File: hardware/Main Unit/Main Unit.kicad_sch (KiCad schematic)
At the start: 1 part

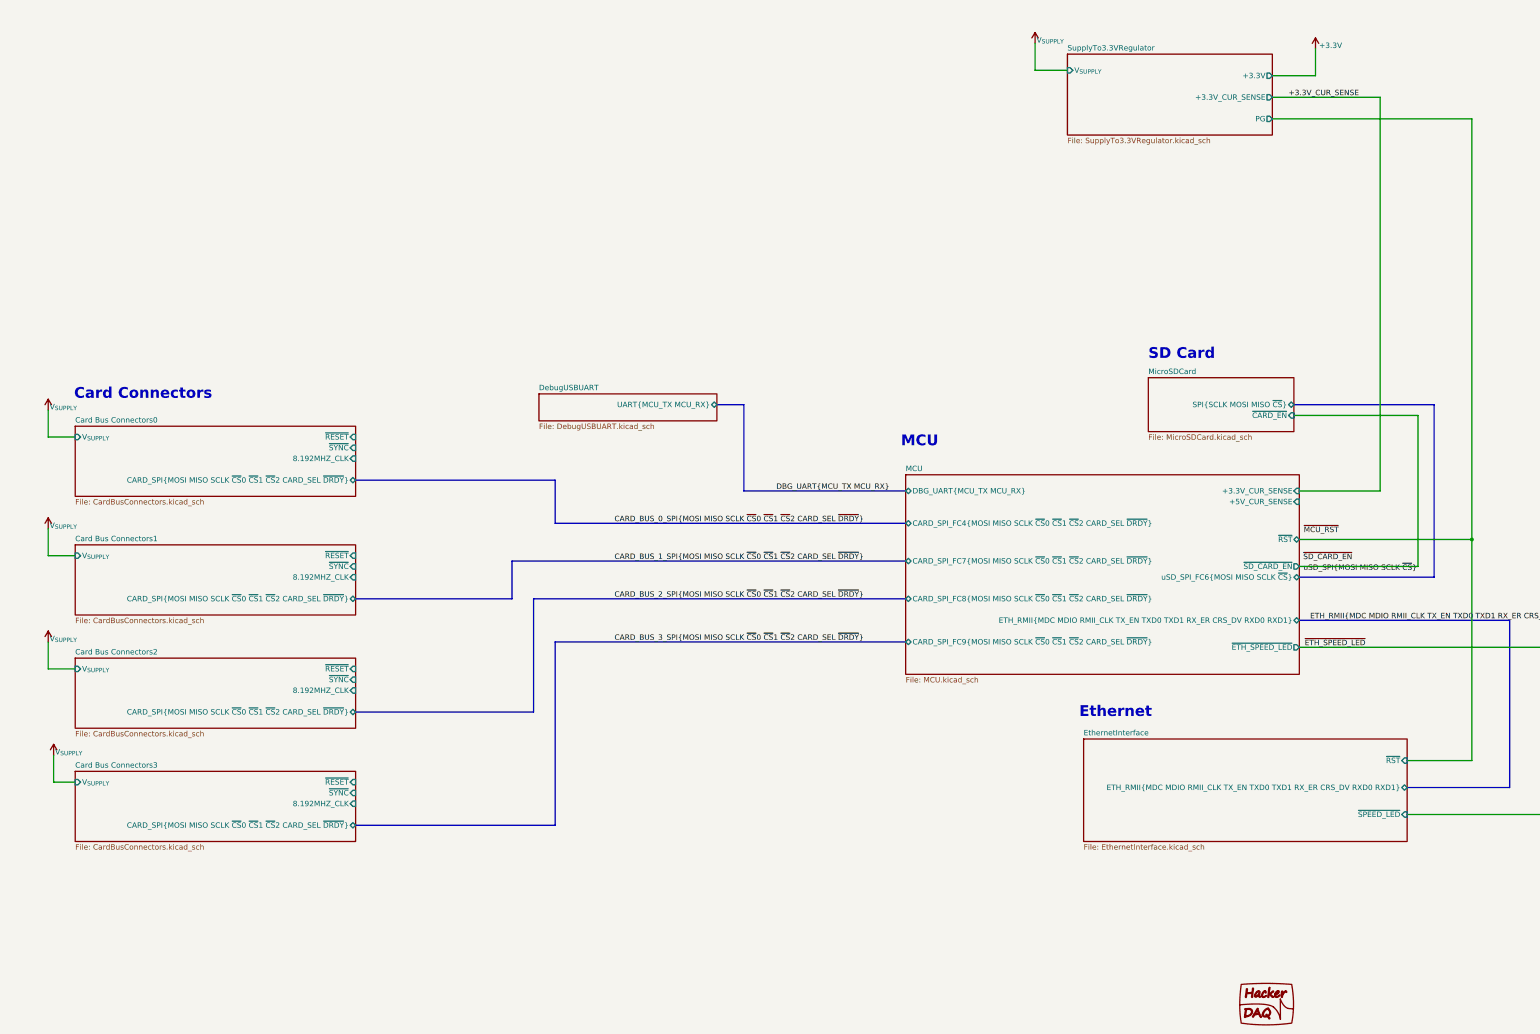
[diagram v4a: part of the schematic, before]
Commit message: Main unit: Add USB port for MCU and 3.3VA rail, start on routing
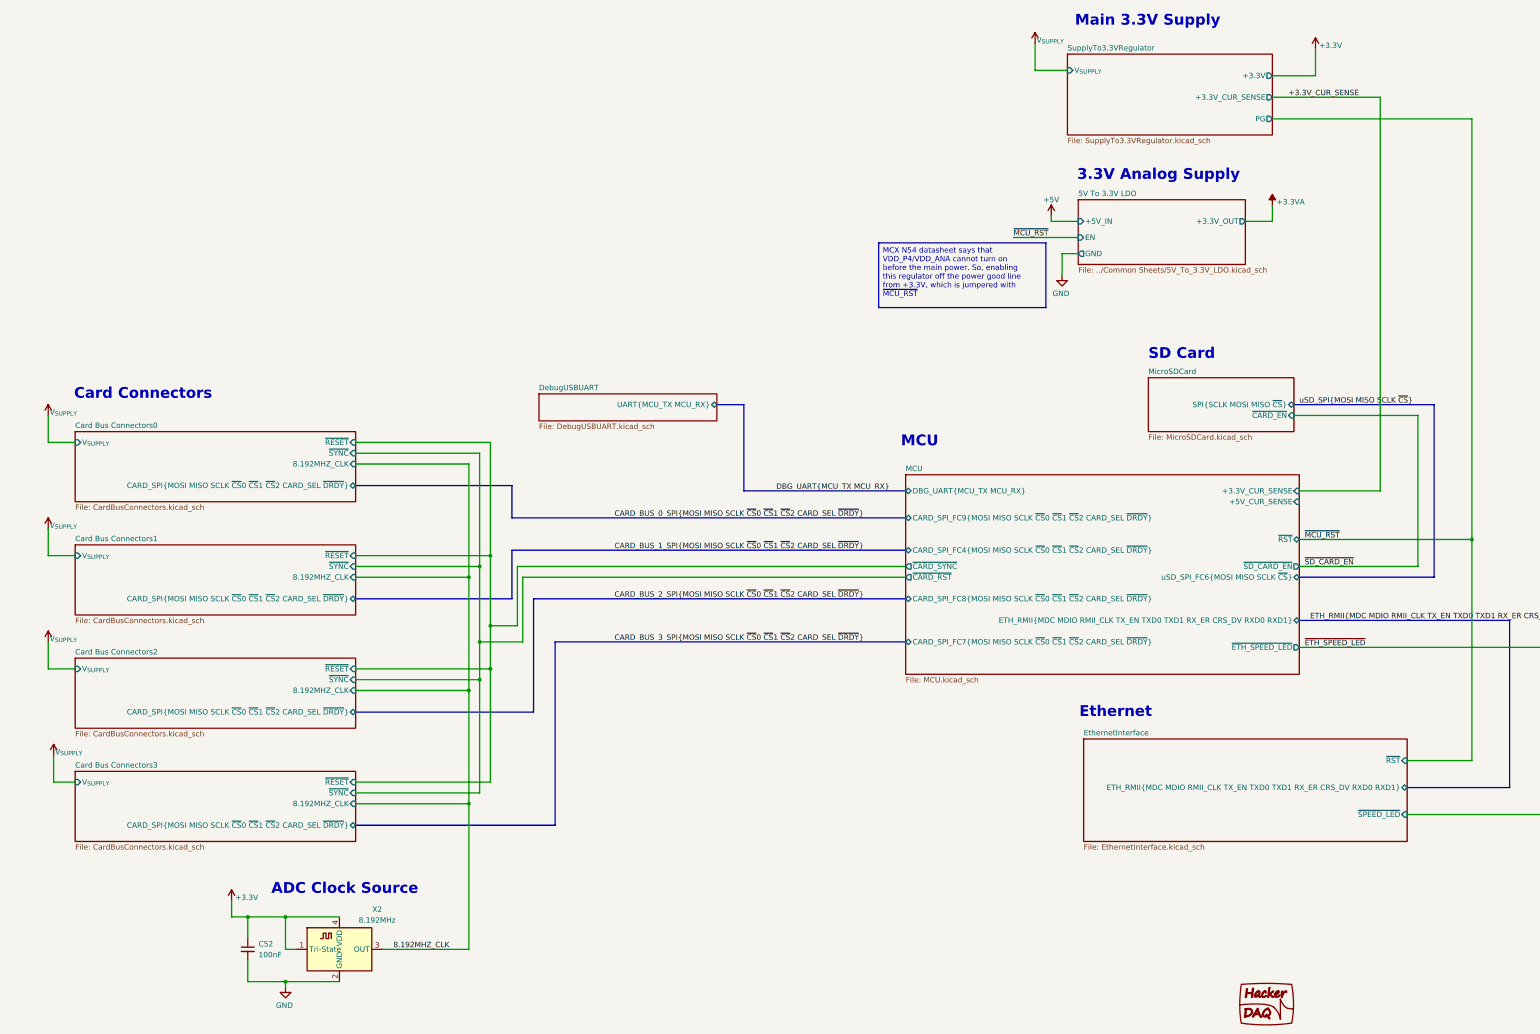
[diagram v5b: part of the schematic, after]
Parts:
- added C52: 100nF, Capacitor_SMD:C_0603_1608Metric, symbol Device:C_Small
- added X2: 8.192MHz, Oscillator:Oscillator_SMD_ECS_2520MV-xxx-xx-4Pin_2.5x2.0mm, symbol Oscillator:ECS-2520MV-xxx-xx
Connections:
- net +3.3V: now also C52.1, X2.1 (Tri-State), X2.4 (VDD)
- new net 8.192MHZ_CLK: X2.3 (OUT)
- new net GND: C52.2, X2.2 (GND)
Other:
- added sheet 5V To 3.3V LDO (../Common Sheets/5V_To_3.3V_LDO.kicad_sch)
- sheet MCU ports: added ~{CARD_RST}, ~{CARD_SYNC}; removed none
- note added: "3.3V Analog Supply"
- note added: "ADC Clock Source"
- note added: "Main 3.3V Supply"

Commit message: Add schematic for Vsupply input
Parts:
- added TP2: +3.3VA, TestPoint:TestPoint_THTPad_D2.5mm_Drill1.2mm, symbol Connector:TestPoint
- added TP3: +3.3V, TestPoint:TestPoint_THTPad_D2.5mm_Drill1.2mm, symbol Connector:TestPoint
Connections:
- net +3.3V: now also TP3.1
- net +3.3VA: now also TP2.1
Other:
- added sheet V_{SUPPLY} Input (VsupplyInput.kicad_sch)
- sheet MCU ports: added V_{SUPPLY}_CUR_SENSE; removed none
- note added: "Power Input"
- note added: "USB to UART for Debugging and Flashing"
